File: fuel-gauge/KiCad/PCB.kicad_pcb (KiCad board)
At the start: 2 copper layers, 100.1 x 70 mm, 41 parts, among them P1 CONN_01X04, P2 CONN_01X04, P3 CONN_01X04, P4 CONN_01X02, Q1 BSS84, Q2 BSS138, Q3 2N7002, SW1 Switch_SPDT_x2, U1 AQV252G, U2 SN74LVC1G08DBVR, U3 TLV3691IDCKR, U4 bq34z100pw

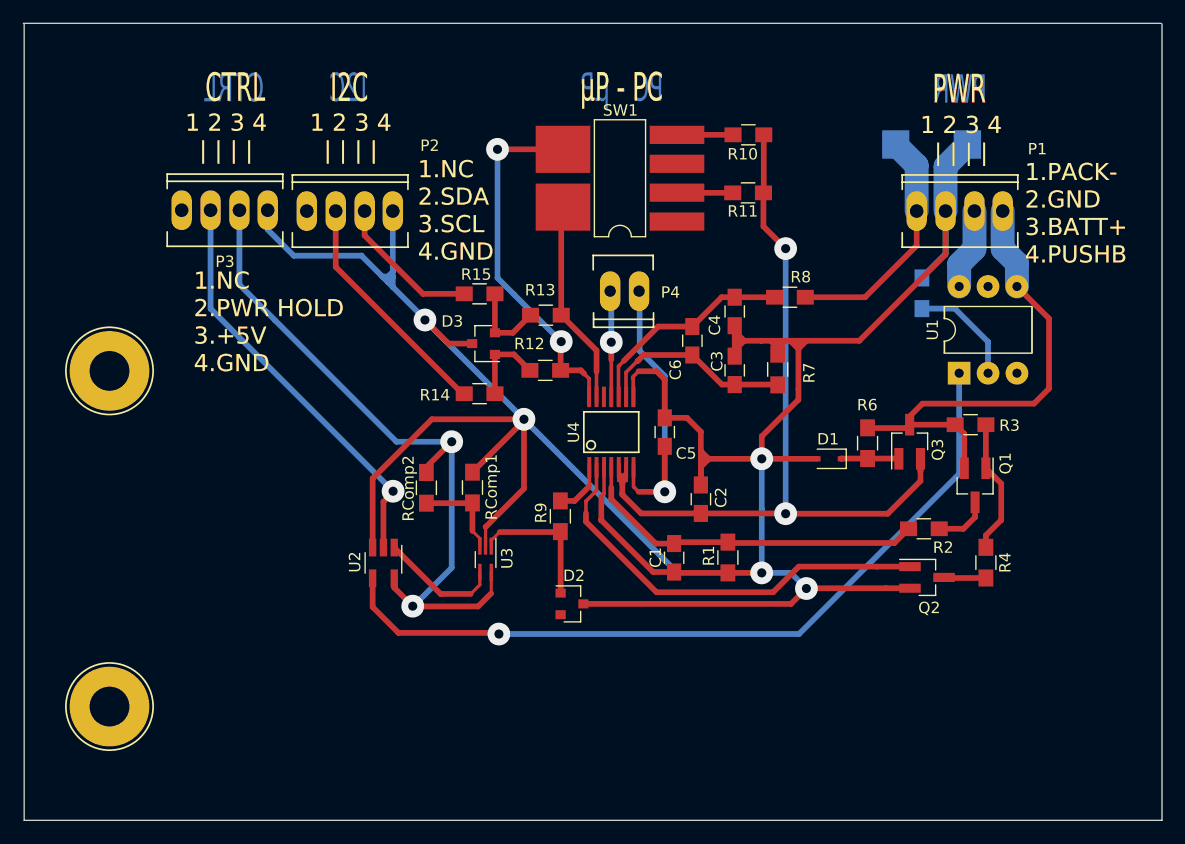
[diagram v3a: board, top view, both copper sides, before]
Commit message: Fix some errors in the border of boards to panelize them correctly
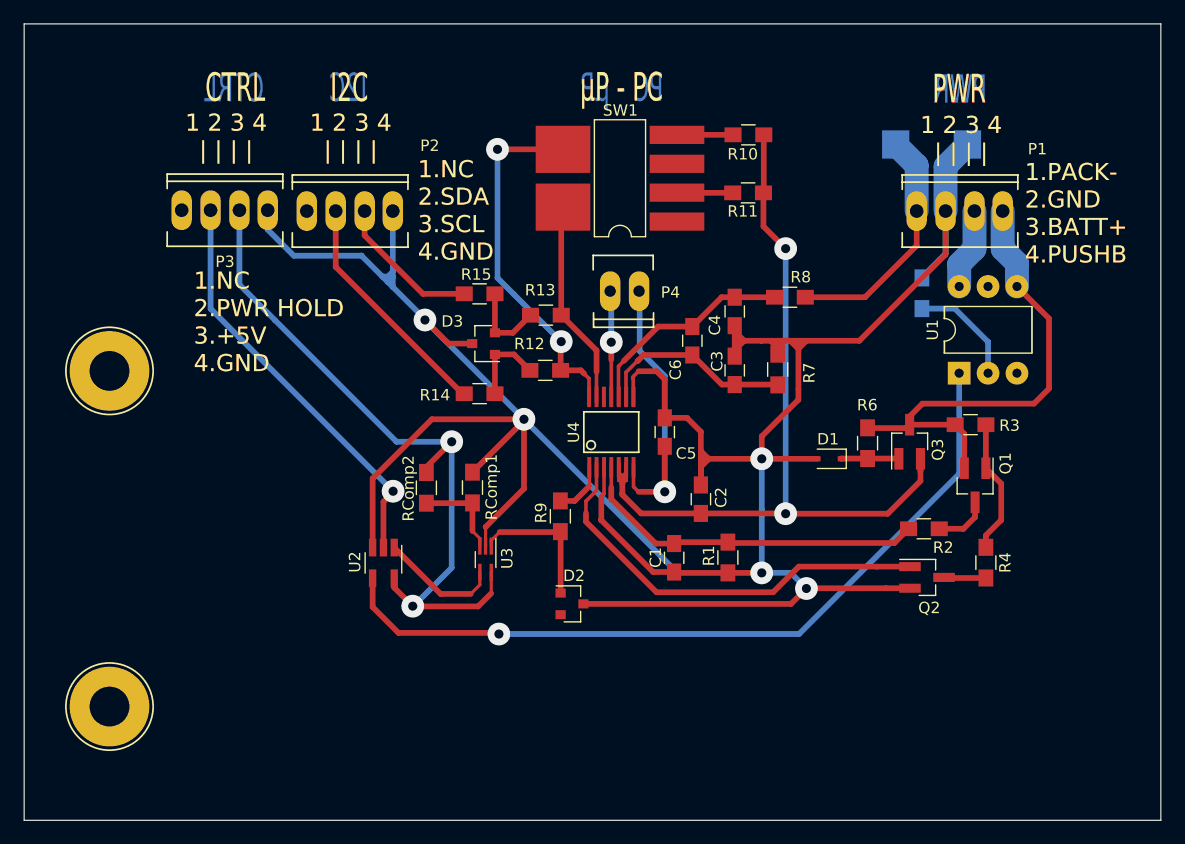
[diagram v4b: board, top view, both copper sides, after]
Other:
- board size 100.1 x 70 mm -> 99.9 x 70 mm
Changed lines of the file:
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@@
     (area 88.57143 49.899999 218.428572 144.700001)
     (thickness 1.6)
-    (drawings 46)
+    (drawings 48)
     (tracks 354)
     (zones 0)
@@
     (pad_drill 0.6)
     (pad_to_mask_clearance 0.1)
-    (aux_axis_origin 0 0)
+    (aux_axis_origin 99.95 130.05)
     (visible_elements 7FFEFE69)
     (pcbplotparams
@@
     )
   )
+  (gr_line (start 199.9 60) (end 100 60) (angle 90) (layer Edge.Cuts) (width 0.1))
+  (gr_line (start 100 130) (end 199.9 130) (angle 90) (layer Edge.Cuts) (width 0.1))
+  (dimension 100 (width 0.3) (layer Margin)
+    (gr_text 100,000mm (at 149.95 137.7) (layer Margin)
+      (effects (font (size 1.5 1.5) (thickness 0.3)))
+    )
+    (feature1 (pts (xy 99.95 129.95) (xy 99.95 139.05)))
+    (feature2 (pts (xy 199.95 129.95) (xy 199.95 139.05)))
+    (crossbar (pts (xy 199.95 136.35) (xy 99.95 136.35)))
+    (arrow1a (pts (xy 99.95 136.35) (xy 101.076504 135.763579)))
+    (arrow1b (pts (xy 99.95 136.35) (xy 101.076504 136.936421)))
+    (arrow2a (pts (xy 199.95 136.35) (xy 198.823496 135.763579)))
+    (arrow2b (pts (xy 199.95 136.35) (xy 198.823496 136.936421)))
+  )
+  (dimension 100.1 (width 0.3) (layer Margin)
+    (gr_text 100,100mm (at 150 133.98) (layer Margin)
+      (effects (font (size 1.5 1.5) (thickness 0.3)))
+    )
+    (feature1 (pts (xy 200.05 129.95) (xy 200.05 135.33)))
+    (feature2 (pts (xy 99.95 129.95) (xy 99.95 135.33)))
+    (crossbar (pts (xy 99.95 132.63) (xy 200.05 132.63)))
+    (arrow1a (pts (xy 200.05 132.63) (xy 198.923496 133.216421)))
+    (arrow1b (pts (xy 200.05 132.63) (xy 198.923496 132.043579)))
+    (arrow2a (pts (xy 99.95 132.63) (xy 101.076504 133.216421)))
+    (arrow2b (pts (xy 99.95 132.63) (xy 101.076504 132.043579)))
+  )
   (gr_text PWR (at 182.2 65.8) (layer F.Cu)
     (effects (font (size 2.5 1.5) (thickness 0.375)))
@@
   )
   (gr_line (start 100 60) (end 100 130) (angle 90) (layer Edge.Cuts) (width 0.1))
-  (gr_line (start 199.925 59.95) (end 99.925 59.95) (angle 90) (layer Edge.Cuts) (width 0.1))
-  (gr_line (start 200 130) (end 200 60) (angle 90) (layer Edge.Cuts) (width 0.1))
+  (gr_line (start 199.9 130) (end 199.9 60) (angle 90) (layer Edge.Cuts) (width 0.1))
   (gr_line (start 110 50) (end 110 135) (angle 90) (layer Margin) (width 0.2))
   (gr_line (start 205 120) (end 95 120) (angle 90) (layer Margin) (width 0.2))
   (gr_line (start 190 50) (end 190 135) (angle 90) (layer Margin) (width 0.2))
-  (gr_line (start 200 130) (end 100 130) (angle 90) (layer Edge.Cuts) (width 0.1))
   (segment (start 177.725 104.375) (end 176.475 105.625) (width 0.5) (layer F.Cu) (net 1))
   (segment (start 176.475 105.625) (end 161.925 105.625) (width 0.5) (layer F.Cu) (net 1))
